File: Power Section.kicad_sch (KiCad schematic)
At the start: 11 parts, among them J1 USB_C_Receptacle_USB2.0, U5 TLV75901PDRVR, U6 USBLC6-2SC6, U8 BQ24074RGTR

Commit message: Updated the power section and battery charging IC
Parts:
- removed C17: 10uF, Capacitor_SMD:C_0603_1608Metric, symbol Device:C_Small
- removed C18: 100nF, Capacitor_SMD:C_0603_1608Metric, symbol Device:C_Small
- removed U5: TLV75901PDRVR, Package_SON:WSON-6-1EP_2x2mm_P0.65mm_EP1x1.6mm, symbol Schematic Symbols:TLV75901PDRVR
- added B1, B2: PESD5V5C1BLYL, PESD5V5C1BLYL(ES):DFN1006-2L-BI-1, symbol PESD5V5C1BLYL(ES):PESD5V5C1BLYL
- added C17, C18, C74: 4.7uF, PCM_JLCPCB:C_0805, symbol PCM_JLCPCB-Capacitors:0805,4.7uF
- added C71, C72, C73: 10uF, Capacitor_SMD:C_0603_1608Metric, symbol Device:C_Small
- added C75: 1uF, PCM_JLCPCB:C_0805, symbol PCM_JLCPCB-Capacitors:0805,1uF
- added C76, C77: 100nF, Capacitor_SMD:C_0603_1608Metric, symbol Device:C_Small
- added C79, C80, C82, C83: 100nF, PCM_JLCPCB:C_0603, symbol PCM_JLCPCB-Capacitors:0603,100nF
- added C81: 10uF, PCM_JLCPCB:C_0805, symbol PCM_JLCPCB-Capacitors:0805,10uF
- added CN1: S2B-PH-SM4-TB, S2B-PH-SM4-TB(LF)(SN):CONN-SMD_P2.00_S2B-PH-SM4-TB-LF-SN, symbol S2B-PH-SM4-TB(LF)(SN):S2B-PH-SM4-TB
- added D59, D60: LED, LED_SMD:LED_0603_1608Metric, symbol Device:LED_Small
- added D74: MMSZ5231B-7-F, MMSZ5231B-7-F:SOD-123_L2.8-W1.8-LS3.7-RD, symbol MMSZ5231B-7-F:MMSZ5231B-7-F
- added D86: SS54F, PCM_JLCPCB:D_SMAF, symbol PCM_JLCPCB-Diodes:Schottky,SS54F
- added L2: BLM18PG121SN1D, BLM18PG121SN1D:L0603, symbol BLM18PG121SN1D:BLM18PG121SN1D_C14709
- added Q2: SSM3J328R,LF, SSM3J328R,LF:SOT-23-3_L2.9-W1.6-P1.90-LS2.8-BR, symbol SSM3J328R,LF:SSM3J328R,LF
- added R35: 10k, Resistor_SMD:R_0402_1005Metric, symbol Device:R_Small
- added R36, R37: 1k, Resistor_SMD:R_0402_1005Metric, symbol Device:R_Small
- added R38: 7.5k, Resistor_SMD:R_0402_1005Metric, symbol Device:R_Small
- added R39, R40, R41: 10k, Resistor_SMD:R_0603_1608Metric, symbol Device:R_Small
- added R43: 47kΩ, PCM_JLCPCB:R_0603, symbol PCM_JLCPCB-Resistors:0603,47kΩ
- added R44: 68kΩ, PCM_JLCPCB:R_0603, symbol PCM_JLCPCB-Resistors:0603,68kΩ
- added R45, R47: 100kΩ, PCM_JLCPCB:R_0603, symbol PCM_JLCPCB-Resistors:0603,100kΩ
- added R46: 200kΩ, PCM_JLCPCB:R_0603, symbol PCM_JLCPCB-Resistors:0603,200kΩ
- added TP11, TP15, TP4, TP5: TestPoint, TestPoint:TestPoint_Pad_D1.5mm, symbol Connector:TestPoint
- added U15: TPS63031DSK, Package_SON:WSON-10-1EP_2.5x2.5mm_P0.5mm_EP1.2x2mm, symbol Regulator_Switching:TPS63031DSK
- added U16: LPS3015-152MRC, LPS3015-152MRC:IND-SMD_L3.0-W3.0_LPS3015-222ML, symbol LPS3015-152MRC:LPS3015-152MRC
- added U17: MAX17048, Abhishek_Library:SON50P200X200X80-9N, symbol PCM_marbastlib-various:MAX17048
- C16: value 10uF -> 100nF; JLCPCB Part # C19702 -> (none)
- R7: value 100K -> 1.18k; JLCPCB Part # C25741 -> (none)
- R8: value 20K -> 1.13k; JLCPCB Part # C25765 -> (none)
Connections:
- net Earth is gone; now on net GND: U6.2 (GND)
- net +3V3: now also R39.1, R40.1, R41.1, TP15.1; no longer R7.1
- net GND: now also R7.1, U8.14 (TMR), U8.17 (EP), U8.4 (~{CE}), U8.6 (EN1), U8.8 (VSS), B1.1 (IO1), B2.1 (IO1), C17.2, C18.2, C71.2, C72.2, C73.2, C74.2, C75.2, C76.2, C77.2, C79.2, C80.2, C81.2, C82.2, C83.2, CN1.2, CN1.3, CN1.4, R35.2, R38.2, R44.2, R45.2, R47.2, TP11.1, U15.11 (PGND), U15.3 (PGND), U15.9 (GND), U17.1 (CTG), U17.4 (GND), U17.6 (QSTRT), U17.9 (GND)
- net VBUS: now also U8.13 (IN), C75.1, C80.1, L2.2, R43.1; no longer C16.1, J1.A4 (VBUS), J1.A9 (VBUS), J1.B4 (VBUS), J1.B9 (VBUS)
- net at R7.2: now also U8.12 (ILIM); no longer R8.1
- net at U8.1 (TS): now also R35.1
- net +VSW: now reaches U8.10 (OUT)
- net +VSW: now also U8.11 (OUT), U8.5 (EN2), C17.1, C71.1, R36.2, R37.2, U15.5 (VIN)
- net at U8.15 (ITERM): now also R38.1
- net at U8.16 (ISET): now also R8.1
- net +BATT: now reaches U8.2 (BAT)
- net +BATT: now also U8.3 (BAT), C18.1, C74.1, C76.1, C77.1, C81.1, C83.1, D74.1 (K), Q2.2 (S), R46.1, U17.2 (CELL), U17.3 (VDD)
- net at U8.7 (~{PGOOD}): now also D60.1 (K)
- net at U8.9 (~{CHG}): now also D59.1 (K)
- new net: D60.2 (A), R37.1
- new net: D59.2 (A), R36.1
- new net: D86.2, J1.A4 (VBUS), J1.A9 (VBUS), J1.B4 (VBUS), J1.B9 (VBUS)
- new net: B1.2 (IO2), C79.1, D86.1, L2.1
- new net: D74.2 (A), Q2.1 (G), R45.1
- new net: B2.2 (IO2), CN1.1, Q2.3 (D)
- new net: U15.2 (L2), U16.1
- new net: U15.4 (L1), U16.2
- new net: C16.1, U15.6 (EN), U15.7 (PS/SYNC), U15.8 (VINA)
- new net ALERT: R39.2, U17.5 (~{ALRT})
- new net ESP_3V3: C72.1, C73.1, U15.1 (VOUT), U15.10 (FB)
- new net I2C0_SCL: R40.2, TP5.1, U17.7 (SCL)
- new net I2C0_SDA: R41.2, TP4.1, U17.8 (SDA)
- new net VADC: C82.1, R46.2, R47.1
- new net usb_vbus_det: R43.2, R44.1
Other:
- note added: "+VBATT = 4.2V VADC_MAX = 100k/(100k+200k)*4.2V ="
- note added: "3V3 Buck-Boost Converter"
- note added: "ADC"
- note added: "Battery Charging IC"
- note added: "Lipo Fuel Gauge"
- note added: "Pull-ups"
- note added: "reverse polarity protection"
- note removed: "VOUT = VFB × (1 + R1/ R2)"
- moved on the sheet: J1, R5, R6, U6, U8

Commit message: Updated the schematic, including power section and the MCU
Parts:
- removed C17, C18, C74: 4.7uF, PCM_JLCPCB:C_0805, symbol PCM_JLCPCB-Capacitors:0805,4.7uF
- removed C75: 1uF, PCM_JLCPCB:C_0805, symbol PCM_JLCPCB-Capacitors:0805,1uF
- removed D59, D60: LED, LED_SMD:LED_0603_1608Metric, symbol Device:LED_Small
- removed R38: 7.5k, Resistor_SMD:R_0402_1005Metric, symbol Device:R_Small
- removed U8: BQ24074RGTR, BQ24074RGTR:QFN-16_L3.0-W3.0-P0.50-TL-EP1.7, symbol BQ24074RGTR:BQ24074RGTR
- added C17: 22uF, Capacitor_SMD:C_1206_3216Metric, symbol Device:C_Small
- added C18, C85: 1uF, Capacitor_SMD:C_0603_1608Metric, symbol Device:C_Small
- added C74: 10uF, Capacitor_SMD:C_1206_3216Metric, symbol Device:C_Small
- added C75, C84: 100nF, Capacitor_SMD:C_0603_1608Metric, symbol Device:C_Small
- added D59, D60: LED, LED_SMD:LED_0603_1608Metric, symbol Device:LED
- added L3: SMMS0630-2R2M, SMMS0630-2R2M:IND-SMD_L6.6-W6.6, symbol SMMS0630-2R2M:SMMS0630-2R2M
- added R3: 2k, Resistor_SMD:R_0402_1005Metric, symbol Device:R_Small
- added U5: MP2617AGL-Z, MP2617AGL-Z:QFN-20_L4.0-W3.0-P0.50_MP2625BGL, symbol MP2617AGL-Z:MP2617AGL-Z
- R35: footprint Resistor_SMD:R_0402_1005Metric -> Resistor_SMD:R_0603_1608Metric
- R36: value 1k -> 10k; footprint Resistor_SMD:R_0402_1005Metric -> Resistor_SMD:R_0603_1608Metric
- R37: value 1k -> 2k
- R7: value 1.18k -> 30.9k; footprint Resistor_SMD:R_0402_1005Metric -> Resistor_SMD:R_0603_1608Metric
- R8: value 1.13k -> 1.05k; footprint Resistor_SMD:R_0402_1005Metric -> Resistor_SMD:R_0603_1608Metric
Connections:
- net +BATT: now also C17.1, U5.14 (BATT)
- net GND: now also R7.2, C17.2, C18.2, C74.2, C75.2, C85.2, U5.11 (AGND), U5.5 (PGND); no longer R7.1
- net VBUS: now also C18.1, C74.1, U5.3 (IN)
- net VCC: now reaches R37.1
- net VCC: now also R36.1, C85.1, R3.1, U5.20 (VCC)
- net at R35.1: now also R36.2, U5.16 (NTC)
- net at R8.1: now also U5.15 (ISET)
- net +VSW renamed SYS
- net SYS: now also L3.1, U5.13 (SYS); no longer R36.2, R37.2
- new net: C84.1, L3.2, U5.2 (SW), U5.4 (SW)
- new net: C84.2, U5.1 (BST)
- new net: D59.1 (K), U5.10 (~{ACOK})
- new net: D59.2 (A), R3.2
- new net: R7.1, U5.17 (ILIM)
- new net: C75.1, U5.18 (TMR)
- new net: D60.1 (K), U5.9 (~{CHGOK})
- new net: D60.2 (A), R37.2
- no-connect marks 2 -> 3
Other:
- moved on the sheet: C81

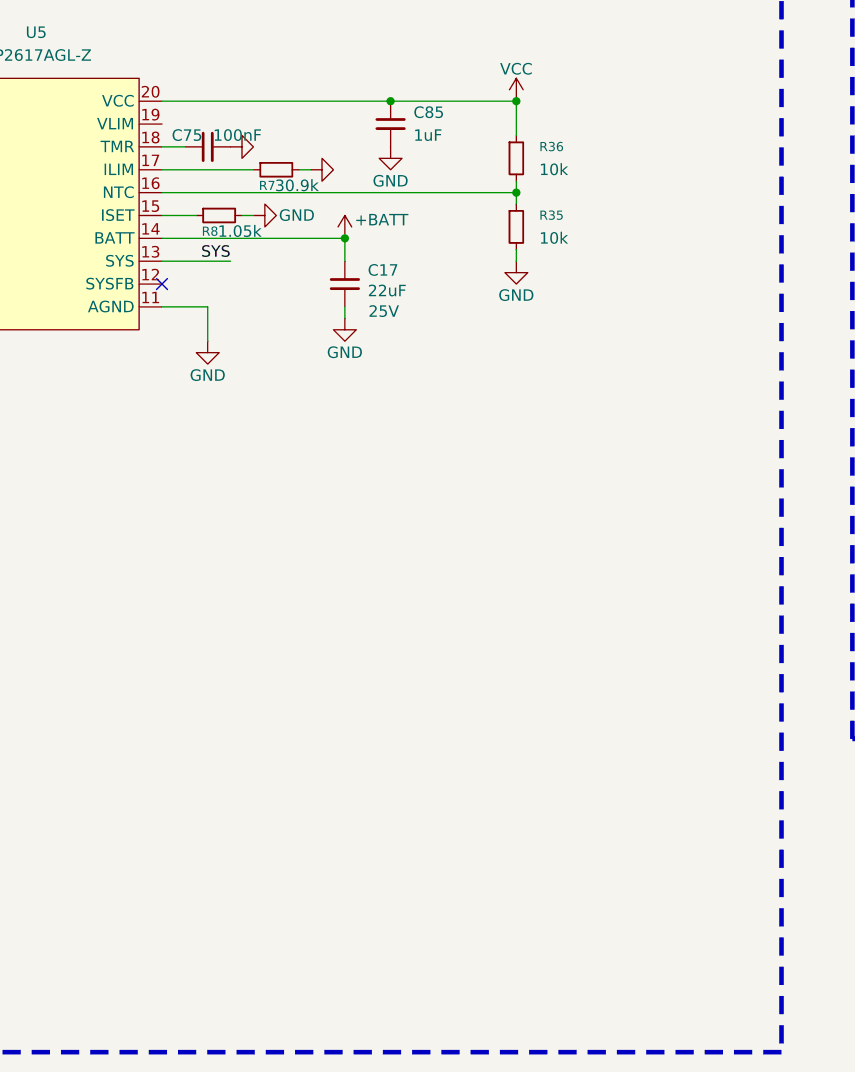
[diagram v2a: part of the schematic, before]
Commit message: Progress with battery charging IC sizing
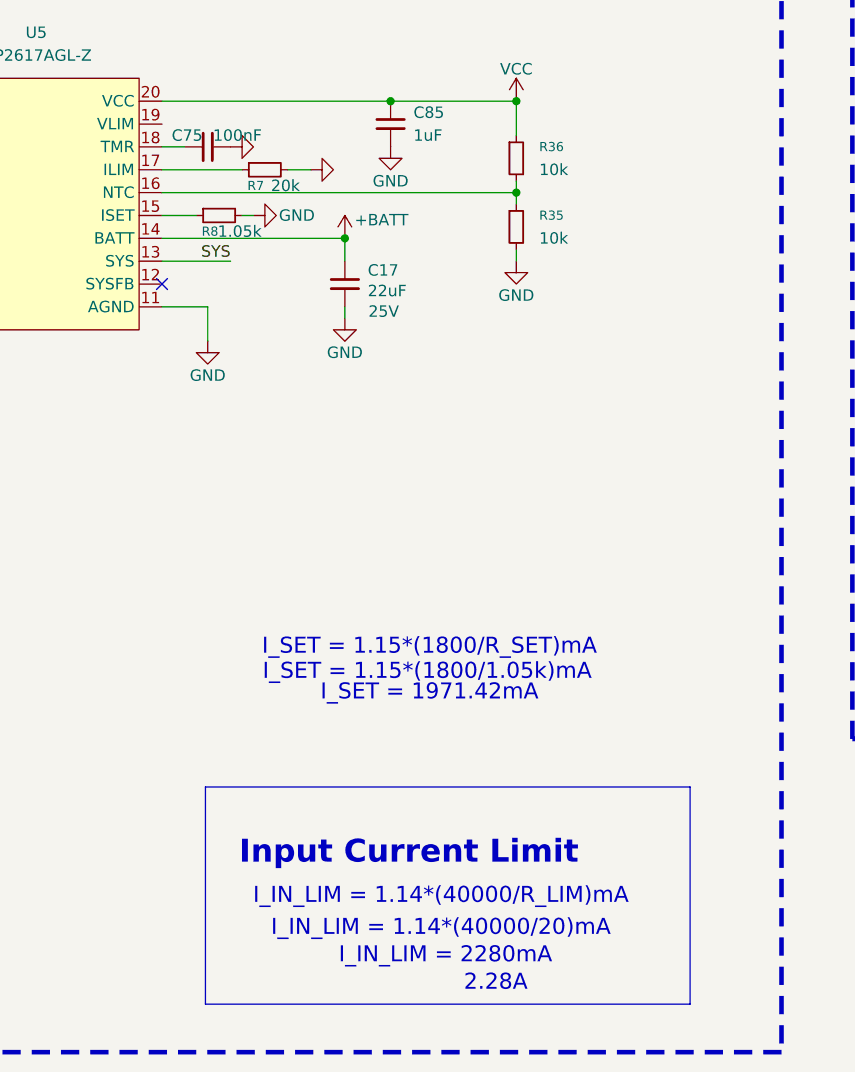
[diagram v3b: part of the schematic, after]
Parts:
- R7: value 30.9k -> 20k
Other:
- note added: "2.28A"
- note added: "I_IN_LIM = 1.14*(40000/20)mA"
- note added: "I_IN_LIM = 1.14*(40000/R_LIM)mA"
- note added: "I_IN_LIM = 2280mA"
- note added: "I_SET = 1.15*(1800/1.05k)mA"
- note added: "I_SET = 1.15*(1800/R_SET)mA"
- note added: "I_SET = 1971.42mA"
- note added: "Input Current Limit"
- moved on the sheet: R7
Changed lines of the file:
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@@
 	)
 	(rectangle
+		(start 143.256 247.65)
+		(end 197.104 271.78)
+		(stroke
+			(width 0)
+			(type default)
+		)
+		(fill
+			(type none)
+		)
+	)
+	(rectangle
 		(start 215.138 132.08)
 		(end 284.734 242.316)
@@
 		)
 	)
+	(text "2.28A"
+		(exclude_from_sim no)
+		(at 175.514 269.494 0)
+		(effects
+			(font
+				(size 1.778 1.778)
+			)
+		)
+	)
+	(text "I_SET = 1.15*(1800/R_SET)mA "
+		(exclude_from_sim no)
+		(at 168.148 232.156 0)
+		(effects
+			(font
+				(size 1.778 1.778)
+			)
+		)
+	)
 	(text "ADC"
 		(exclude_from_sim no)
@@
 		)
 	)
+	(text "I_SET = 1971.42mA "
+		(exclude_from_sim no)
+		(at 168.148 237.236 0)
+		(effects
+			(font
+				(size 1.778 1.778)
+			)
+		)
+	)
+	(text "I_IN_LIM = 1.14*(40000/R_LIM)mA "
+		(exclude_from_sim no)
+		(at 169.418 259.842 0)
+		(effects
+			(font
+				(size 1.778 1.778)
+			)
+		)
+	)
+	(text "I_SET = 1.15*(1800/1.05k)mA "
+		(exclude_from_sim no)
+		(at 167.894 234.95 0)
+		(effects
+			(font
+				(size 1.778 1.778)
+			)
+		)
+	)
+	(text "I_IN_LIM = 2280mA "
+		(exclude_from_sim no)
+		(at 169.926 266.446 0)
+		(effects
+			(font
+				(size 1.778 1.778)
+			)
+		)
+	)
 	(text "+VBATT = 4.2V\nVADC_MAX = 100k/(100k+200k)*4.2V = "
 		(exclude_from_sim no)
@@
 		)
 	)
+	(text "I_IN_LIM = 1.14*(40000/20)mA "
+		(exclude_from_sim no)
+		(at 169.418 263.398 0)
+		(effects
+			(font
+				(size 1.778 1.778)
+			)
+		)
+	)
 	(text "reverse polarity protection"
 		(exclude_from_sim no)
@@
 		)
 	)
+	(text "Input Current Limit"
+		(exclude_from_sim no)
+		(at 165.862 255.016 0)
+		(effects
+			(font
+				(size 2.54 2.54)
+				(thickness 0.508)
+				(bold yes)
+				(color 204 102 0 1)
+			)
+		)
+	)
 	(junction
 		(at 152.4 58.42)
@@
 	(wire
 		(pts
-			(xy 138.43 179.07) (xy 148.59 179.07)
+			(xy 138.43 179.07) (xy 147.32 179.07)
 		)
 		(stroke
@@
 	(wire
 		(pts
-			(xy 154.94 179.07) (xy 153.67 179.07)
+			(xy 154.94 179.07) (xy 152.4 179.07)
 		)
 		(stroke
@@
 	(symbol
 		(lib_id "Device:R_Small")
-		(at 151.13 179.07 90)
+		(at 149.86 179.07 90)
 		(mirror x)
 		(unit 1)
@@
 		(dnp no)
 		(property "Reference" "R7"
-			(at 150.114 180.848 90)
+			(at 148.844 180.848 90)
 			(show_name no)
 			(do_not_autoplace no)
@@
 			)
 		)
-		(property "Value" "30.9k"
-			(at 153.416 180.848 90)
+		(property "Value" "20k"
+			(at 152.146 180.848 90)
 			(show_name no)
 			(do_not_autoplace no)
@@
 		)
 		(property "Footprint" "Resistor_SMD:R_0603_1608Metric"
-			(at 151.13 179.07 0)
+			(at 149.86 179.07 0)
 			(hide yes)
 			(show_name no)
@@
 		)
 		(property "Datasheet" ""
-			(at 151.13 179.07 0)
+			(at 149.86 179.07 0)
 			(hide yes)
 			(show_name no)
@@
 		)
 		(property "Description" "Resistor, small symbol"
-			(at 151.13 179.07 0)
+			(at 149.86 179.07 0)
 			(hide yes)
 			(show_name no)
@@
 		)
 		(property "Availability" ""
-			(at 151.13 179.07 90)
+			(at 149.86 179.07 90)
 			(hide yes)
 			(show_name no)
@@
 		)
 		(property "Check_prices" ""
-			(at 151.13 179.07 90)
+			(at 149.86 179.07 90)
 			(hide yes)
 			(show_name no)
@@
 		)
 		(property "Height" ""
-			(at 151.13 179.07 90)
+			(at 149.86 179.07 90)
 			(hide yes)
 			(show_name no)
@@
 		)
 		(property "MF" ""
-			(at 151.13 179.07 90)
+			(at 149.86 179.07 90)
 			(hide yes)
 			(show_name no)
@@
 		)
 		(property "MP" ""
-			(at 151.13 179.07 90)
+			(at 149.86 179.07 90)
 			(hide yes)
 			(show_name no)
@@
 		)
 		(property "Manufacturer_Name" ""
-			(at 151.13 179.07 90)
+			(at 149.86 179.07 90)
 			(hide yes)
 			(show_name no)
@@
 		)
 		(property "Manufacturer_Part_Number" ""
-			(at 151.13 179.07 90)
+			(at 149.86 179.07 90)
 			(hide yes)
 			(show_name no)
@@
 		)
 		(property "Mouser Part Number" ""
-			(at 151.13 179.07 90)
+			(at 149.86 179.07 90)
 			(hide yes)
 			(show_name no)
@@
 		)
 		(property "Mouser Price/Stock" ""
-			(at 151.13 179.07 90)
+			(at 149.86 179.07 90)
 			(hide yes)
 			(show_name no)
@@
 		)
 		(property "Package" ""
-			(at 151.13 179.07 90)
+			(at 149.86 179.07 90)
 			(hide yes)
 			(show_name no)
@@
 		)
 		(property "STANDARD" ""
-			(at 151.13 179.07 90)
+			(at 149.86 179.07 90)
 			(hide yes)
 			(show_name no)
@@
 		)
 		(property "SnapEDA_Link" ""
-			(at 151.13 179.07 90)
+			(at 149.86 179.07 90)
 			(hide yes)
 			(show_name no)
